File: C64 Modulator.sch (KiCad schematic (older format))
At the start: 40 parts, among them J10 , J11 , J12 , J13 , J14 , J2 8765, J3 4321, J4 AUD_STEREO, J5 TRS_3.5mm, J6 RCA_PLUG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

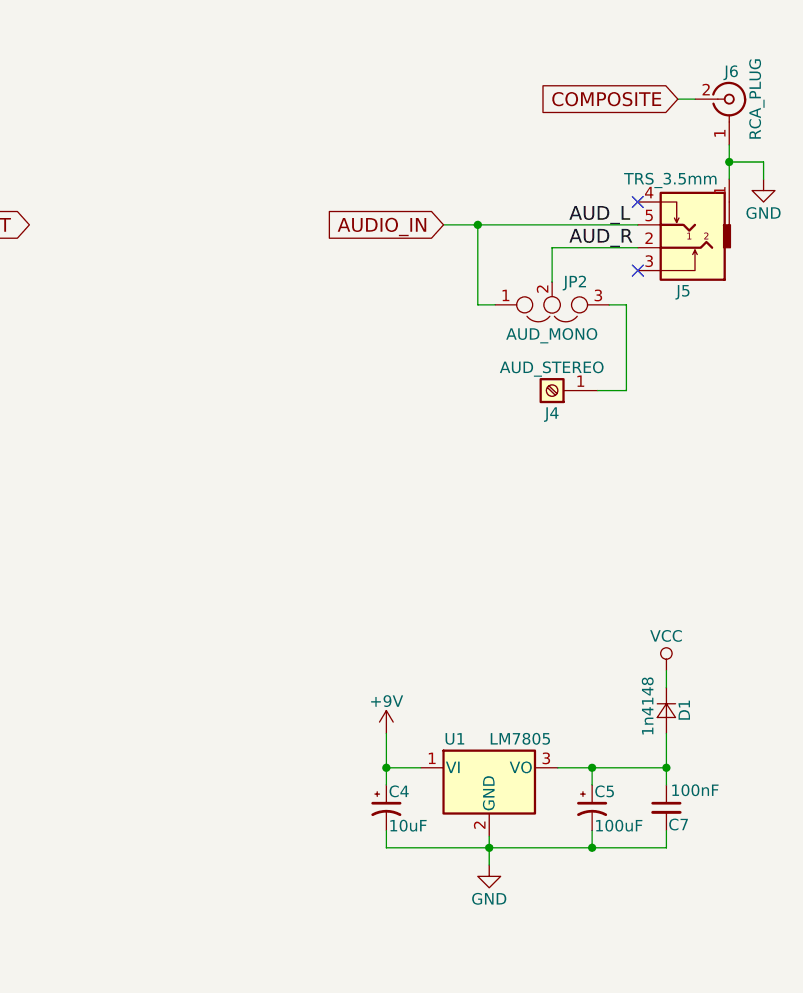
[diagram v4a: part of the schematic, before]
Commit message: Audio decoupling caps on schematic
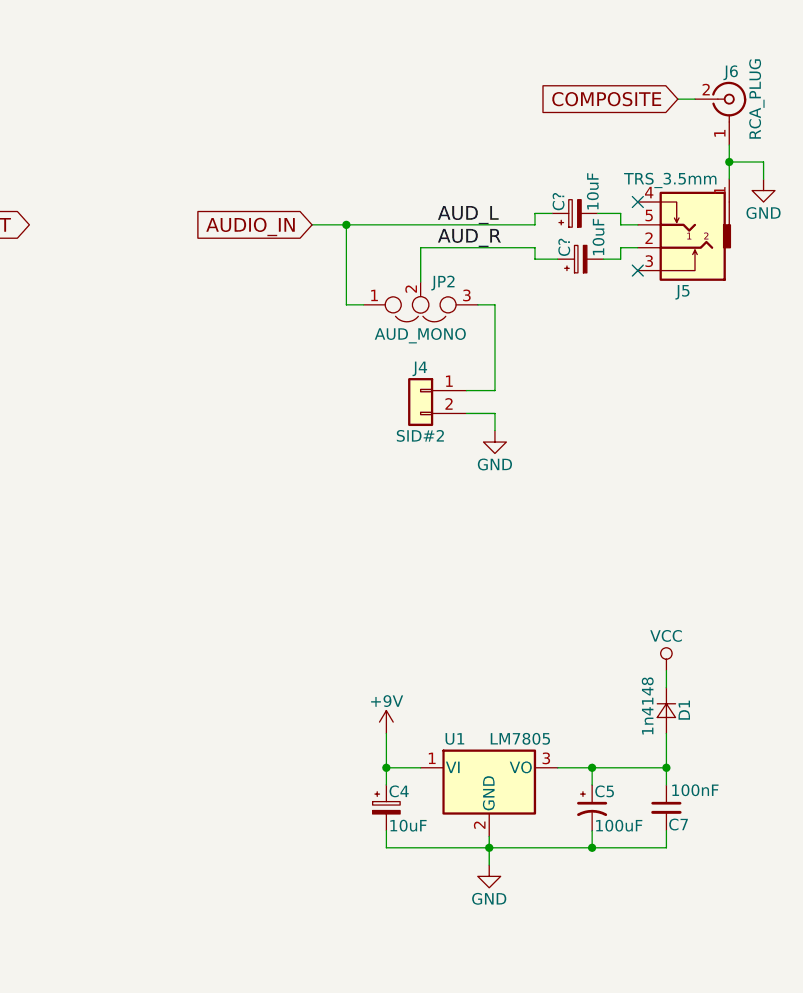
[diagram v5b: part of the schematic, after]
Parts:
- removed C4: 10uF, Capacitors_THT:CP_Radial_D4.0mm_P2.00mm, symbol CP1_Small
- removed J4: AUD_STEREO, Pin_Headers:Pin_Header_Straight_1x01_Pitch2.54mm, symbol Screw_Terminal_01x01
- added C4, C? (x2): 10uF, symbol CP_Small
- added J4: SID#2, symbol Conn_01x02
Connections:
- net +9V: now also C4.1
- net AUDIO_IN: now also C?.1; no longer J5.5
- net AUD_R: now also C?.1; no longer J5.2
- net GND: now also C4.2, J4.2 (Pin_2)
- net at JP2.3: now also J4.1 (Pin_1)
- new net: C?.2, J5.2
- new net: C?.2, J5.5
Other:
- moved on the sheet: JP2
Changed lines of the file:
@@
 NoConn ~ 10075 1750
 NoConn ~ 10075 2050
-Text GLabel 9225 1850 0    60   Input ~ 0
+Text GLabel 8650 1850 0    60   Input ~ 0
 AUDIO_IN
-$Comp
-L Screw_Terminal_01x01 J4
-U 1 1 5D0DC721
-P 9700 2575
-F 0 "J4" H 9700 2675 50  0000 C CNN
-F 1 "AUD_STEREO" H 9700 2475 50  0000 C CNN
-F 2 "Pin_Headers:Pin_Header_Straight_1x01_Pitch2.54mm" H 9700 2575 50  0001 C CNN
-F 3 "" H 9700 2575 50  0001 C CNN
-	1    9700 2575
-	-1   0    0    1
-$EndComp
-Text Label 9775 1850 0    60   ~ 0
+Text Label 9200 1850 0    60   ~ 0
 AUD_L
-Text Label 9775 1950 0    60   ~ 0
+Text Label 9200 1950 0    60   ~ 0
 AUD_R
 Wire Wire Line
-	9225 1850 10075 1850
-Wire Wire Line
-	9700 1950 10075 1950
+	8650 1850 9625 1850
+Wire Wire Line
+	9125 1950 9625 1950
 $Comp
 L Jumper_NC_Dual JP2
 U 1 1 5D0E13BF
-P 9700 2200
-F 0 "JP2" H 9750 2100 50  0000 L CNN
-F 1 "AUD_MONO" H 9700 2300 50  0000 C BNN
-F 2 "Pin_Headers:Pin_Header_Straight_1x03_Pitch2.54mm" H 9700 2200 50  0001 C CNN
-F 3 "" H 9700 2200 50  0001 C CNN
-	1    9700 2200
+P 9125 2200
+F 0 "JP2" H 9175 2100 50  0000 L CNN
+F 1 "AUD_MONO" H 9125 2300 50  0000 C BNN
+F 2 "Pin_Headers:Pin_Header_Straight_1x03_Pitch2.54mm" H 9125 2200 50  0001 C CNN
+F 3 "" H 9125 2200 50  0001 C CNN
+	1    9125 2200
 	1    0    0    1
 $EndComp
 Wire Wire Line
-	9700 2100 9700 1950
-Wire Wire Line
-	9450 2200 9375 2200
-Wire Wire Line
-	9375 2200 9375 1850
-Connection ~ 9375 1850
-Wire Wire Line
-	9950 2200 10025 2200
-Wire Wire Line
-	10025 2200 10025 2575
-Wire Wire Line
-	10025 2575 9900 2575
+	9125 2100 9125 1950
+Wire Wire Line
+	8875 2200 8800 2200
+Wire Wire Line
+	8800 2200 8800 1850
+Connection ~ 8800 1850
+Wire Wire Line
+	9375 2200 9450 2200
+Wire Wire Line
+	9450 2200 9450 2575
+Wire Wire Line
+	9450 2575 9325 2575
 $Comp
 L GND #PWR06
@@
 	1    0    0    -1
 $EndComp
-$Comp
-L CP1_Small C4
-U 1 1 5D4BB37A
-P 8975 4400
-F 0 "C4" H 8985 4470 50  0000 L CNN
-F 1 "10uF" H 8985 4320 50  0000 L CNN
-F 2 "Capacitors_THT:CP_Radial_D4.0mm_P2.00mm" H 8975 4400 50  0001 C CNN
-F 3 "" H 8975 4400 50  0001 C CNN
-	1    8975 4400
-	1    0    0    -1
-$EndComp
 Wire Wire Line
 	9125 4225 8975 4225
@@
 Wire Wire Line
 	10200 3800 10200 3875
+$Comp
+L CP_Small C?
+U 1 1 5D556521
+P 9800 1800
+F 0 "C?" H 9810 1870 50  0000 L CNN
+F 1 "10uF" H 9810 1720 50  0000 L CNN
+F 2 "" H 9800 1800 50  0001 C CNN
+F 3 "" H 9800 1800 50  0001 C CNN
+	1    9800 1800
+	0    -1   -1   0
+$EndComp
+$Comp
+L CP_Small C?
+U 1 1 5D556B7D
+P 9825 2000
+F 0 "C?" H 9835 2070 50  0000 L CNN
+F 1 "10uF" H 9835 1920 50  0000 L CNN
+F 2 "" H 9825 2000 50  0001 C CNN
+F 3 "" H 9825 2000 50  0001 C CNN
+	1    9825 2000
+	0    -1   -1   0
+$EndComp
+Wire Wire Line
+	9625 1850 9625 1800
+Wire Wire Line
+	9625 1800 9700 1800
+Wire Wire Line
+	9725 2000 9625 2000
+Wire Wire Line
+	9625 2000 9625 1950
+Wire Wire Line
+	9900 1800 10000 1800
+Wire Wire Line
+	10000 1800 10000 1850
+Wire Wire Line
+	10000 1850 10075 1850
+Wire Wire Line
+	10075 1950 10000 1950
+Wire Wire Line
+	10000 1950 10000 2000
+Wire Wire Line
+	10000 2000 9925 2000
+$Comp
+L Conn_01x02 J4
+U 1 1 5D55784F
+P 9125 2575
+F 0 "J4" H 9125 2675 50  0000 C CNN
+F 1 "SID#2" H 9125 2375 50  0000 C CNN
+F 2 "" H 9125 2575 50  0001 C CNN
+F 3 "" H 9125 2575 50  0001 C CNN
+	1    9125 2575
+	-1   0    0    -1
+$EndComp
+$Comp
+L GND #PWR?
+U 1 1 5D55B688
+P 9450 2750
+F 0 "#PWR?" H 9450 2500 50  0001 C CNN
+F 1 "GND" H 9450 2600 50  0000 C CNN
+F 2 "" H 9450 2750 50  0001 C CNN
+F 3 "" H 9450 2750 50  0001 C CNN
+	1    9450 2750
+	1    0    0    -1
+$EndComp
+Wire Wire Line
+	9450 2750 9450 2675
+Wire Wire Line
+	9450 2675 9325 2675
+$Comp
+L CP_Small C4
+U 1 1 5D55EB7A
+P 8975 4400
+F 0 "C4" H 8985 4470 50  0000 L CNN
+F 1 "10uF" H 8985 4320 50  0000 L CNN
+F 2 "" H 8975 4400 50  0001 C CNN
+F 3 "" H 8975 4400 50  0001 C CNN
+	1    8975 4400
+	1    0    0    -1
+$EndComp
 $EndSCHEMATC

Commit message: Assigned updated footprints
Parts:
- C4: footprint (none) -> Capacitors_THT:CP_Radial_D5.0mm_P2.50mm
- C8, C9: renamed from C?; footprint (none) -> Capacitors_THT:CP_Radial_D5.0mm_P2.50mm
- J4: footprint (none) -> Pin_Headers:Pin_Header_Straight_1x02_Pitch2.54mm
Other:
- note added: "B"
- note added: "Based on the C64 RF-modulator mod by Zero-X / OMS, this simply adapts those\nschematics with changes of my own to create a complete replacement for the\nmodulator. Given differences in pinouts this variant is meant for installation only on\nCommodore 64s with "longboards"."
- note added: "C64 Modulator replacement, "Longboard" edition"
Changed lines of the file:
@@
 	10200 3800 10200 3875
 $Comp
-L CP_Small C?
+L CP_Small C8
 U 1 1 5D556521
 P 9800 1800
-F 0 "C?" H 9810 1870 50  0000 L CNN
+F 0 "C8" H 9810 1870 50  0000 L CNN
 F 1 "10uF" H 9810 1720 50  0000 L CNN
-F 2 "" H 9800 1800 50  0001 C CNN
+F 2 "Capacitors_THT:CP_Radial_D5.0mm_P2.50mm" H 9800 1800 50  0001 C CNN
 F 3 "" H 9800 1800 50  0001 C CNN
 	1    9800 1800
@@
 $EndComp
 $Comp
-L CP_Small C?
+L CP_Small C9
 U 1 1 5D556B7D
 P 9825 2000
-F 0 "C?" H 9835 2070 50  0000 L CNN
+F 0 "C9" H 9835 2070 50  0000 L CNN
 F 1 "10uF" H 9835 1920 50  0000 L CNN
-F 2 "" H 9825 2000 50  0001 C CNN
+F 2 "Capacitors_THT:CP_Radial_D5.0mm_P2.50mm" H 9825 2000 50  0001 C CNN
 F 3 "" H 9825 2000 50  0001 C CNN
 	1    9825 2000
@@
 F 0 "J4" H 9125 2675 50  0000 C CNN
 F 1 "SID#2" H 9125 2375 50  0000 C CNN
-F 2 "" H 9125 2575 50  0001 C CNN
+F 2 "Pin_Headers:Pin_Header_Straight_1x02_Pitch2.54mm" H 9125 2575 50  0001 C CNN
 F 3 "" H 9125 2575 50  0001 C CNN
 	1    9125 2575
@@
 $EndComp
 $Comp
-L GND #PWR?
+L GND #PWR011
 U 1 1 5D55B688
 P 9450 2750
-F 0 "#PWR?" H 9450 2500 50  0001 C CNN
+F 0 "#PWR011" H 9450 2500 50  0001 C CNN
 F 1 "GND" H 9450 2600 50  0000 C CNN
 F 2 "" H 9450 2750 50  0001 C CNN
@@
 F 0 "C4" H 8985 4470 50  0000 L CNN
 F 1 "10uF" H 8985 4320 50  0000 L CNN
-F 2 "" H 8975 4400 50  0001 C CNN
+F 2 "Capacitors_THT:CP_Radial_D5.0mm_P2.50mm" H 8975 4400 50  0001 C CNN
 F 3 "" H 8975 4400 50  0001 C CNN
 	1    8975 4400
 	1    0    0    -1
 $EndComp
+Text Notes 7000 6950 0    60   ~ 0
+Based on the C64 RF-modulator mod by Zero-X / OMS, this simply adapts those\nschematics with changes of my own to create a complete replacement for the\nmodulator. Given differences in pinouts this variant is meant for installation only on\nCommodore 64s with "longboards".
+Text Notes 7350 7500 0    60   ~ 0
+C64 Modulator replacement, "Longboard" edition
+Text Notes 10550 7650 0    60   ~ 0
+B
 $EndSCHEMATC

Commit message: Updated PCB layout
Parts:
- J4: value SID#2 -> AUD_RIGHT
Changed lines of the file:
@@
 P 9125 2575
 F 0 "J4" H 9125 2675 50  0000 C CNN
-F 1 "SID#2" H 9125 2375 50  0000 C CNN
+F 1 "AUD_RIGHT" H 9125 2375 50  0000 C CNN
 F 2 "Pin_Headers:Pin_Header_Straight_1x02_Pitch2.54mm" H 9125 2575 50  0001 C CNN
 F 3 "" H 9125 2575 50  0001 C CNN

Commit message: Removed C8/C9
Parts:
- removed C8, C9: 10uF, Capacitors_THT:CP_Radial_D5.0mm_P2.50mm, symbol CP_Small
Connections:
- net AUDIO_IN: now also J5.5
- net AUD_R: now also J5.2
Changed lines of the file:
@@
 AUD_R
 Wire Wire Line
-	8650 1850 9625 1850
-Wire Wire Line
-	9125 1950 9625 1950
+	8650 1850 10075 1850
+Wire Wire Line
+	9125 1950 10075 1950
 $Comp
 L Jumper_NC_Dual JP2
@@
 	10200 3800 10200 3875
 $Comp
-L CP_Small C8
-U 1 1 5D556521
-P 9800 1800
-F 0 "C8" H 9810 1870 50  0000 L CNN
-F 1 "10uF" H 9810 1720 50  0000 L CNN
-F 2 "Capacitors_THT:CP_Radial_D5.0mm_P2.50mm" H 9800 1800 50  0001 C CNN
-F 3 "" H 9800 1800 50  0001 C CNN
-	1    9800 1800
-	0    -1   -1   0
-$EndComp
-$Comp
-L CP_Small C9
-U 1 1 5D556B7D
-P 9825 2000
-F 0 "C9" H 9835 2070 50  0000 L CNN
-F 1 "10uF" H 9835 1920 50  0000 L CNN
-F 2 "Capacitors_THT:CP_Radial_D5.0mm_P2.50mm" H 9825 2000 50  0001 C CNN
-F 3 "" H 9825 2000 50  0001 C CNN
-	1    9825 2000
-	0    -1   -1   0
-$EndComp
-Wire Wire Line
-	9625 1850 9625 1800
-Wire Wire Line
-	9625 1800 9700 1800
-Wire Wire Line
-	9725 2000 9625 2000
-Wire Wire Line
-	9625 2000 9625 1950
-Wire Wire Line
-	9900 1800 10000 1800
-Wire Wire Line
-	10000 1800 10000 1850
-Wire Wire Line
-	10000 1850 10075 1850
-Wire Wire Line
-	10075 1950 10000 1950
-Wire Wire Line
-	10000 1950 10000 2000
-Wire Wire Line
-	10000 2000 9925 2000
-$Comp
 L Conn_01x02 J4
